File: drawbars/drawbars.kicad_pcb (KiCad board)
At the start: 2 copper layers, 234 x 87 mm, 55 parts, among them J1 8-215079-6, J2 8-215079-6, J3 8-215079-6, Q1 BC547, U1 4051, U2 4051, U3 74HC04

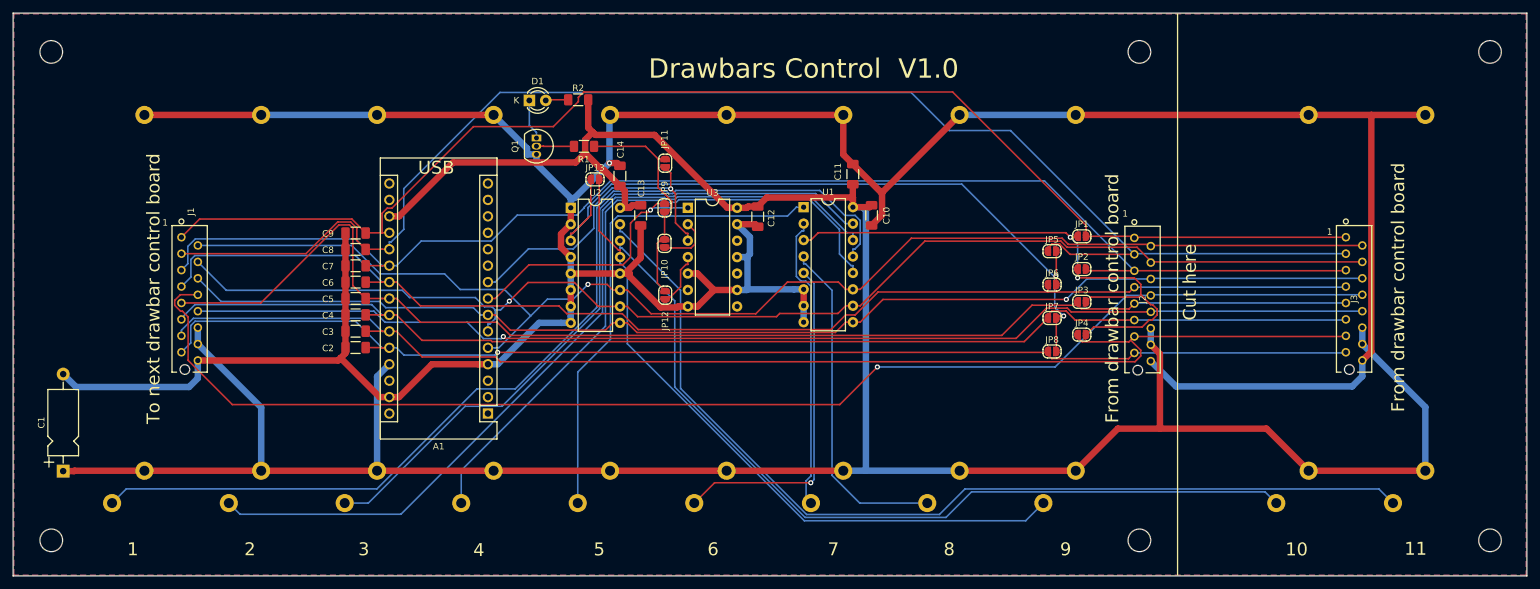
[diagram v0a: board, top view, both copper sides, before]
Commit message: Drawbars Rev 1.1
On schematics : UP_REG_LED and LO_REG_LED signals were not routed to connectors.
Connectors pins assignments modified.
On PCB : Cutting line width increased. PCB width smaller for better drawbars 8 digit visibility when drawbars are pulled to max.
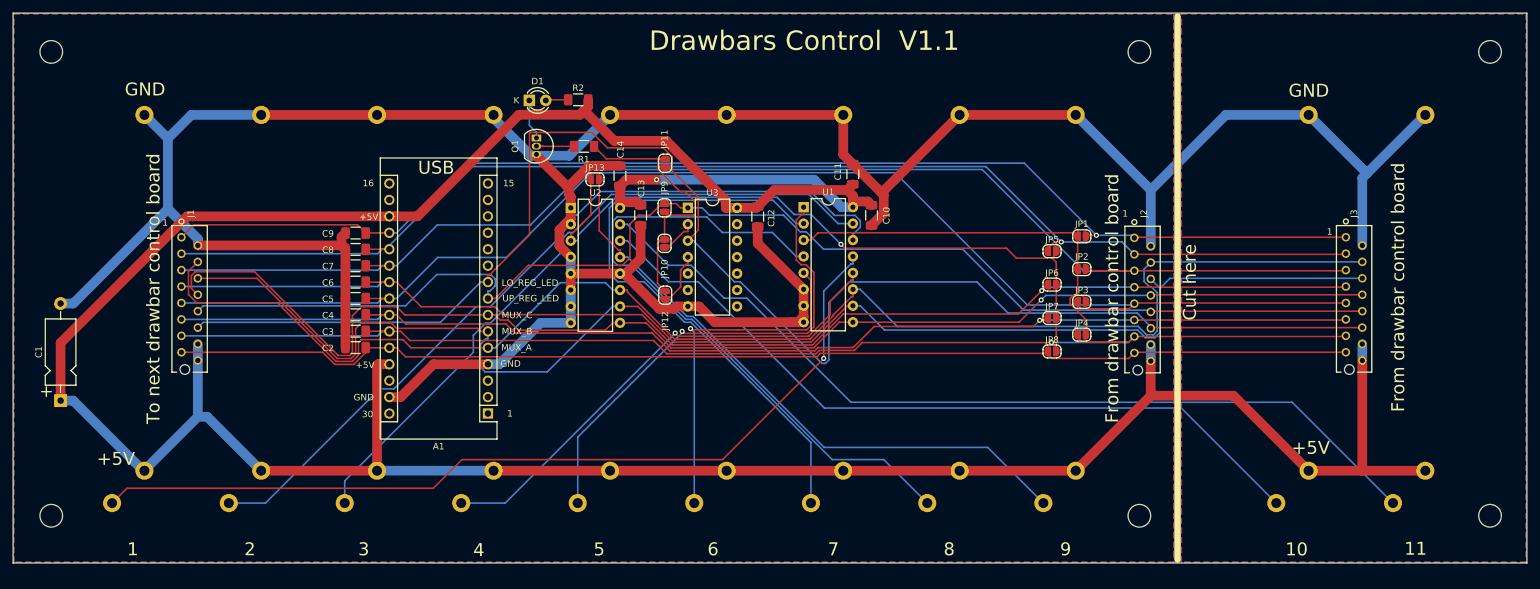
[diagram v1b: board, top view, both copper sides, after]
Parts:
- moved C1 10.9 mm to (38.3, 101.9)
- moved REF4 3.80 mm to (259.3, 119.7)
- moved REF5 3.80 mm to (205.1, 119.7)
- moved REF6 3.80 mm to (36.9, 119.7)
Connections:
- A1 pad 8: /UP_KB_LED -> /UP_REG_LED
- A1 pad 9: /LO_KB_LED -> /LO_REG_LED
- J1 pad 10: /MUX_B -> /MUX_A
- J1 pad 11: /MUX_C -> /MUX_B
- J1 pad 12: /UPPER_LED -> /MUX_C
- J1 pad 13: /LOWER_LED -> /UP_REG_LED
- J1 pad 14: +5V -> /LO_REG_LED
- J1 pad 16: GND -> +5V
- J1 pad 9: /MUX_A -> GND
- J2 pad 10: /MUX_B -> /MUX_A
- J2 pad 11: /MUX_C -> /MUX_B
- J2 pad 12: /UPPER_LED -> /MUX_C
- J2 pad 13: /LOWER_LED -> /UP_REG_LED
- J2 pad 14: +5V -> /LO_REG_LED
- J2 pad 16: GND -> +5V
- J2 pad 9: /MUX_A -> GND
- J3 pad 10: /MUX_B -> /MUX_A
- J3 pad 11: /MUX_C -> /MUX_B
- J3 pad 12: /UPPER_LED -> /MUX_C
- J3 pad 13: /LOWER_LED -> /UP_REG_LED
- J3 pad 14: +5V -> /LO_REG_LED
- J3 pad 16: GND -> +5V
- J3 pad 9: /MUX_A -> GND
- JP11 pad 1: /LO_KB_LED -> /LO_REG_LED
- JP9 pad 1: /UP_KB_LED -> /UP_REG_LED
- U3 pad 1: /UP_KB_LED -> /UP_REG_LED
- U3 pad 11: GND -> (no net)
- U3 pad 13: GND -> (no net)
- U3 pad 3: /LO_KB_LED -> /LO_REG_LED
- U3 pad 5: GND -> (no net)
- U3 pad 9: GND -> (no net)
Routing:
- net /LO_REG_LED: track 0.00 -> 239.4 mm
- net /UPPER_LED: track 205.6 -> 0.00 mm, vias 1 -> 0
- net /UP_REG_LED: track 0.00 -> 203.5 mm
- net /LOWER_LED: track 184.2 -> 0.00 mm, vias 1 -> 0
- net Net-(RV8-Pad2): track 52.3 -> 102.6 mm
- net /LO_KB_LED: track 49.3 -> 0.00 mm, vias 1 -> 0
- net Net-(RV7-Pad2): track 45.8 -> 93.5 mm
- net +5V: track 454.2 -> 496.6 mm, vias 0 -> 1
- net /UP_KB_LED: track 42.4 -> 0.00 mm, vias 1 -> 0
- net GND: track 515.7 -> 483.8 mm, vias 1 -> 0
- net /ANLGA: track 88.6 -> 62.1 mm, vias 2 -> 0
- net /ANLG1: track 224.5 -> 198.4 mm, vias 0 -> 1
- net Net-(RV4-Pad2): track 101.1 -> 77.6 mm, vias 0 -> 1
- net /MUX_B: track 197.3 -> 218.5 mm, vias 1 -> 0
- net /MUX_A: track 203.4 -> 222.5 mm, vias 1 -> 0
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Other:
- board size 234 x 87 mm -> 234 x 85 mm
- board text added: "+5V"
- board text added: "15"
- board text added: "16"
- board text added: "30"
- board text added: "Drawbars Control V1.1"
- board text added: "GND"
- board text added: "LO_REG_LED"
- board text added: "MUX_A"
- board text added: "MUX_B"
- board text added: "MUX_C"
- board text added: "UP_REG_LED"
- board text removed: "Drawbars Control V1.0"
